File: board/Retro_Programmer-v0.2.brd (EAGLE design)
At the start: 45 x 45 mm, 48 parts, among them IC1 74LVC125A, K1 61301511821, K2 61301511821, P1 POWERSUPPLY_DC21MMX, Q1 BC857CSMD, Q2 BC847, SW1 SPUSH, SW2 SPUSH, SW3 SPUSH, SW4 SLIDE_WAY4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

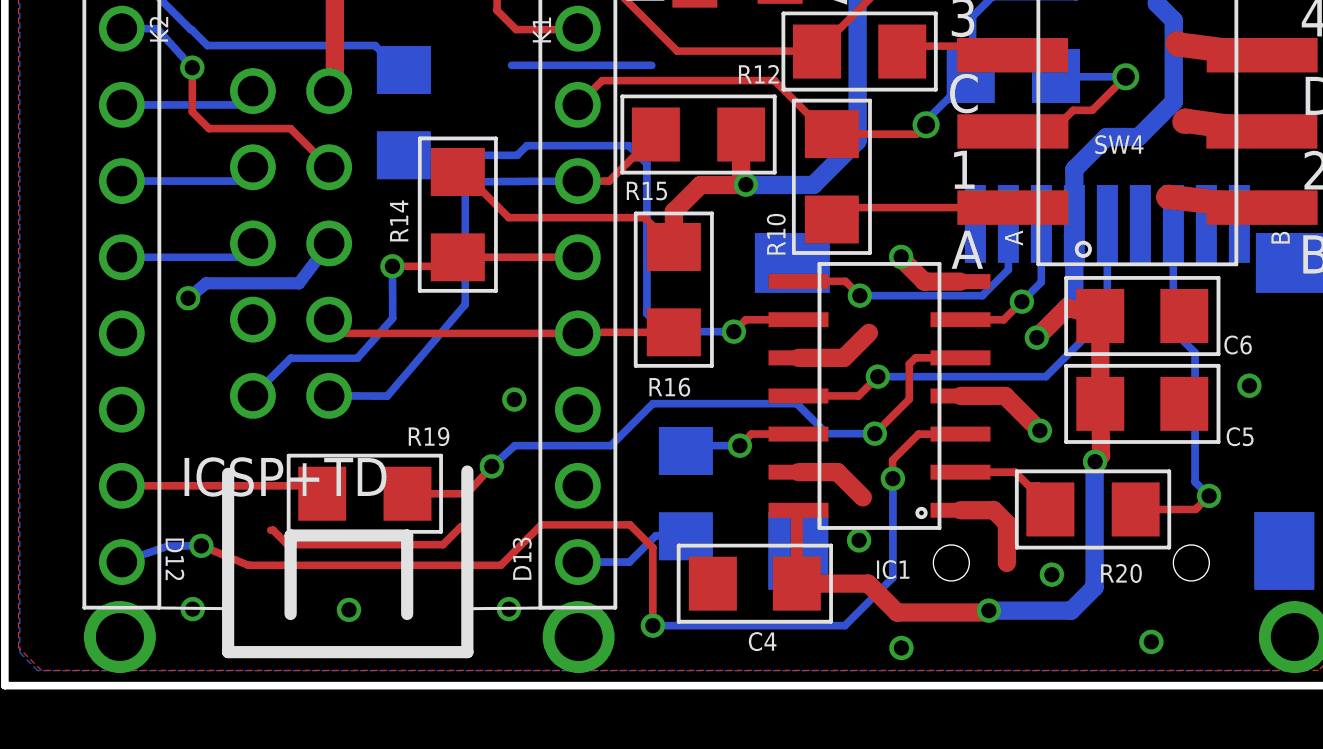
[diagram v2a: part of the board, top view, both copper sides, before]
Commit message: Board: Fixed ICSP+TID label, and other labels
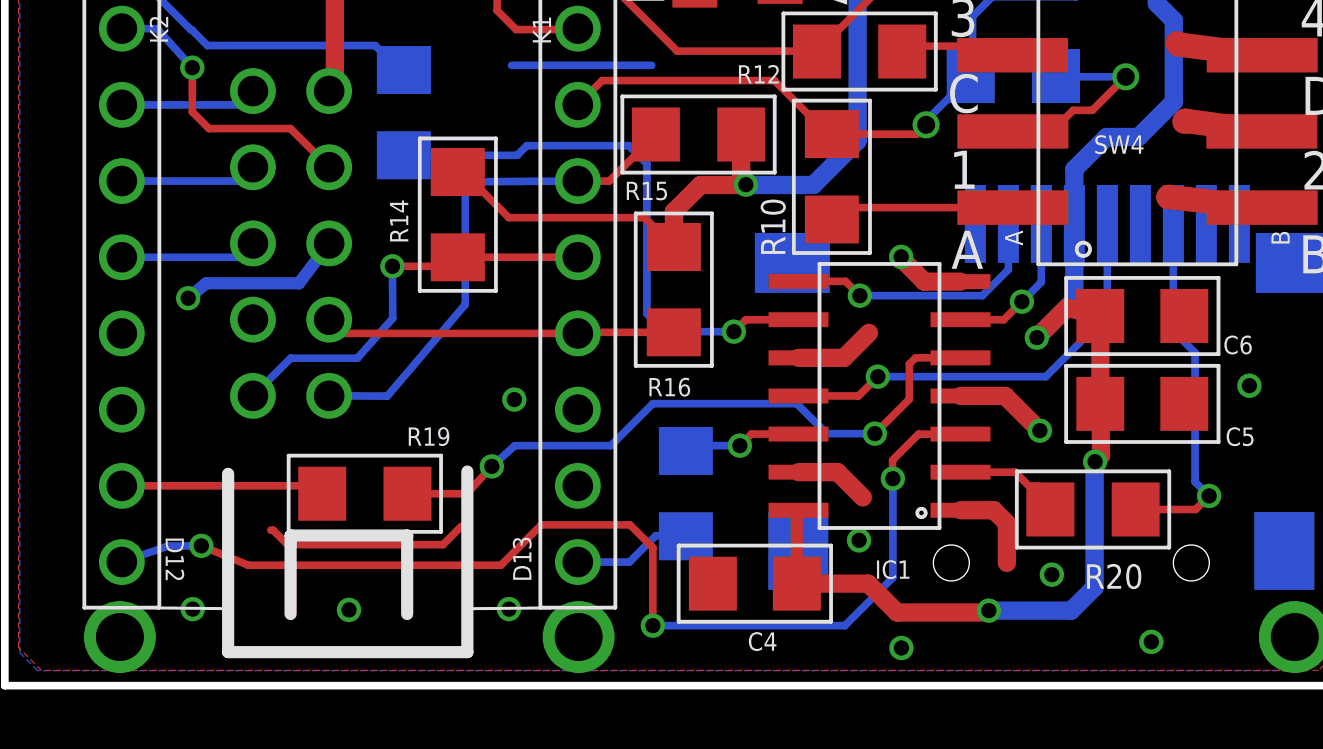
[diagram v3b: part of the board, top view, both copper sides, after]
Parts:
- renumbered ICSP+TD to ICSP+TID
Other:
- board text added: "10"
- board text added: "5"
- board text added: "6"
- board text added: "7"
- board text added: "8"
- board text added: "9"
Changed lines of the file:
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@@
 <layers>
 <layer number="1" name="Top" color="4" fill="1" visible="yes" active="yes"/>
-<layer number="16" name="Bottom" color="1" fill="1" visible="yes" active="yes"/>
+<layer number="16" name="Bottom" color="1" fill="1" visible="no" active="yes"/>
 <layer number="17" name="Pads" color="2" fill="1" visible="yes" active="yes"/>
 <layer number="18" name="Vias" color="2" fill="1" visible="yes" active="yes"/>
@@
 <text x="5.3848" y="40.386" size="0.6096" layer="25" font="vector" ratio="16" distance="20" rot="SR270">TX1</text>
 <text x="13.208" y="28.7274" size="0.6096" layer="25" font="vector" ratio="16" distance="20">v0.2</text>
+<text x="8.6868" y="21.463" size="1.778" layer="26" rot="MR0">1</text>
+<text x="11.303" y="21.5392" size="1.778" layer="26" rot="MR0">2</text>
+<text x="6.9088" y="16.51" size="1.778" layer="26" rot="MR0">3</text>
+<text x="6.9596" y="14.0208" size="1.778" layer="26" rot="MR0">5</text>
+<text x="13.589" y="11.2776" size="1.778" layer="26" rot="MR0">8</text>
+<text x="13.5382" y="14.3764" size="1.778" layer="26" rot="MR0">6</text>
+<text x="15.0114" y="8.8392" size="1.778" layer="26" rot="MR0">10</text>
+<text x="6.858" y="8.7884" size="1.778" layer="26" rot="MR0">9</text>
+<text x="6.8834" y="11.1506" size="1.778" layer="26" rot="MR0">7</text>
 </plain>
 <attributes>
@@
 <attribute name="VALUE" x="28.6554" y="15.3564" size="0.6096" layer="27" rot="R180"/>
 </element>
-<element name="ICSP+TD" library="Wuerth_Elektronik_Board_to_Board" package="61301021821" value="61301021821" x="9.54" y="14.74" smashed="yes" rot="MR90">
-<attribute name="NAME" x="5.8383" y="6.3214" size="1.27" layer="25"/>
+<element name="ICSP+TID" library="Wuerth_Elektronik_Board_to_Board" package="61301021821" value="61301021821" x="9.54" y="14.74" smashed="yes" rot="MR90">
+<attribute name="NAME" x="13.4329" y="6.3214" size="1.27" layer="26" rot="MR0"/>
 <attribute name="VALUE" x="0.2622" y="3.5528" size="1.27" layer="28" rot="MR90"/>
 </element>
@@
 </element>
 <element name="Q1" library="transistor-pnp" package="SOT23-BEC" value="BC857CSMD" x="15.7" y="34.3" smashed="yes" rot="MR180">
-<attribute name="NAME" x="16.462" y="37.221" size="0.6096" layer="26" rot="MR180"/>
+<attribute name="NAME" x="16.462" y="37.221" size="0.8128" layer="26" rot="MR180"/>
 <attribute name="VALUE" x="13.795" y="37.475" size="1.27" layer="28" rot="MR180"/>
 </element>
@@
 </element>
 <element name="R10" library="rcl" package="R1206" value="22K" x="27.5682" y="16.9618" smashed="yes" rot="R90">
-<attribute name="NAME" x="26.0188" y="14.2948" size="0.6096" layer="25" rot="R90"/>
+<attribute name="NAME" x="26.0188" y="14.2948" size="0.8128" layer="25" rot="R90"/>
 <attribute name="VALUE" x="30.1082" y="15.6918" size="1.27" layer="27" rot="R90"/>
 </element>
@@
 </element>
 <element name="R17" library="rcl" package="R1206" value="3.3K" x="22.7" y="6.4" smashed="yes" rot="MR90">
-<attribute name="NAME" x="23.6144" y="2.9456" size="0.6096" layer="26" rot="MR0"/>
+<attribute name="NAME" x="23.8176" y="2.7932" size="0.8128" layer="26" rot="MR0"/>
 <attribute name="VALUE" x="20.16" y="5.13" size="1.27" layer="28" rot="MR90"/>
 </element>
 <element name="R18" library="rcl" package="R1206" value="3.3K" x="13.3" y="19.1" smashed="yes" rot="MR270">
-<attribute name="NAME" x="15.8146" y="20.4208" size="0.6096" layer="26" rot="MR270"/>
+<attribute name="NAME" x="15.8146" y="20.4208" size="0.8128" layer="26" rot="MR270"/>
 <attribute name="VALUE" x="15.84" y="20.37" size="1.27" layer="28" rot="MR270"/>
 </element>
@@
 </element>
 <element name="R20" library="rcl" package="R1206" value="3.3K" x="36.273" y="5.873" smashed="yes" rot="R180">
-<attribute name="NAME" x="37.9494" y="4.0442" size="0.6096" layer="25" rot="R180"/>
+<attribute name="NAME" x="37.9494" y="4.0442" size="0.8128" layer="25" rot="R180"/>
 <attribute name="VALUE" x="37.543" y="8.413" size="1.27" layer="27" rot="R180"/>
 </element>
@@
 <signal name="A2">
 <contactref element="R15" pad="1"/>
-<contactref element="ICSP+TD" pad="1"/>
+<contactref element="ICSP+TID" pad="1"/>
 <contactref element="K1" pad="10"/>
 <wire x1="19.1" y1="16.82" x2="20.1488" y2="16.82" width="0.254" layer="1"/>
@@
 <signal name="A1">
 <contactref element="R14" pad="1"/>
-<contactref element="ICSP+TD" pad="10"/>
+<contactref element="ICSP+TID" pad="10"/>
 <contactref element="K1" pad="11"/>
 <via x="12.9204" y="13.978" extent="1-16" drill="0.508"/>
@@
 </signal>
 <signal name="A0">
-<contactref element="ICSP+TD" pad="2"/>
+<contactref element="ICSP+TID" pad="2"/>
 <contactref element="R16" pad="1"/>
 <contactref element="K1" pad="12"/>
@@
 </signal>
 <signal name="D5">
-<contactref element="ICSP+TD" pad="4"/>
+<contactref element="ICSP+TID" pad="4"/>
 <contactref element="K2" pad="8"/>
 <wire x1="5.0748" y1="21.9" x2="6.2484" y2="20.5994" width="0.254" layer="16"/>
@@
 </signal>
 <signal name="D6">
-<contactref element="ICSP+TD" pad="6"/>
+<contactref element="ICSP+TID" pad="6"/>
 <contactref element="K2" pad="9"/>
 <wire x1="3.9" y1="19.36" x2="7.81" y2="19.36" width="0.254" layer="16"/>
@@
 </signal>
 <signal name="D7">
-<contactref element="ICSP+TD" pad="7"/>
+<contactref element="ICSP+TID" pad="7"/>
 <contactref element="K2" pad="10"/>
 <wire x1="3.9" y1="16.82" x2="7.81" y2="16.82" width="0.254" layer="16"/>
@@
 </signal>
 <signal name="D8">
-<contactref element="ICSP+TD" pad="8"/>
+<contactref element="ICSP+TID" pad="8"/>
 <contactref element="K2" pad="11"/>
 <wire x1="3.9" y1="14.28" x2="7.81" y2="14.28" width="0.254" layer="16"/>
@@
 <contactref element="U2" pad="GND"/>
 <contactref element="SW3" pad="2"/>
-<contactref element="ICSP+TD" pad="3"/>
+<contactref element="ICSP+TID" pad="3"/>
 <contactref element="C4" pad="2"/>
 <contactref element="IC1" pad="13"/>
@@
 </signal>
 <signal name="D3ENB">
-<contactref element="ICSP+TD" pad="5"/>
+<contactref element="ICSP+TID" pad="5"/>
 <contactref element="Q1" pad="C"/>
 <contactref element="R23" pad="2"/>
